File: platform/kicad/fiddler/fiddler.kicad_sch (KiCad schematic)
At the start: 0 parts

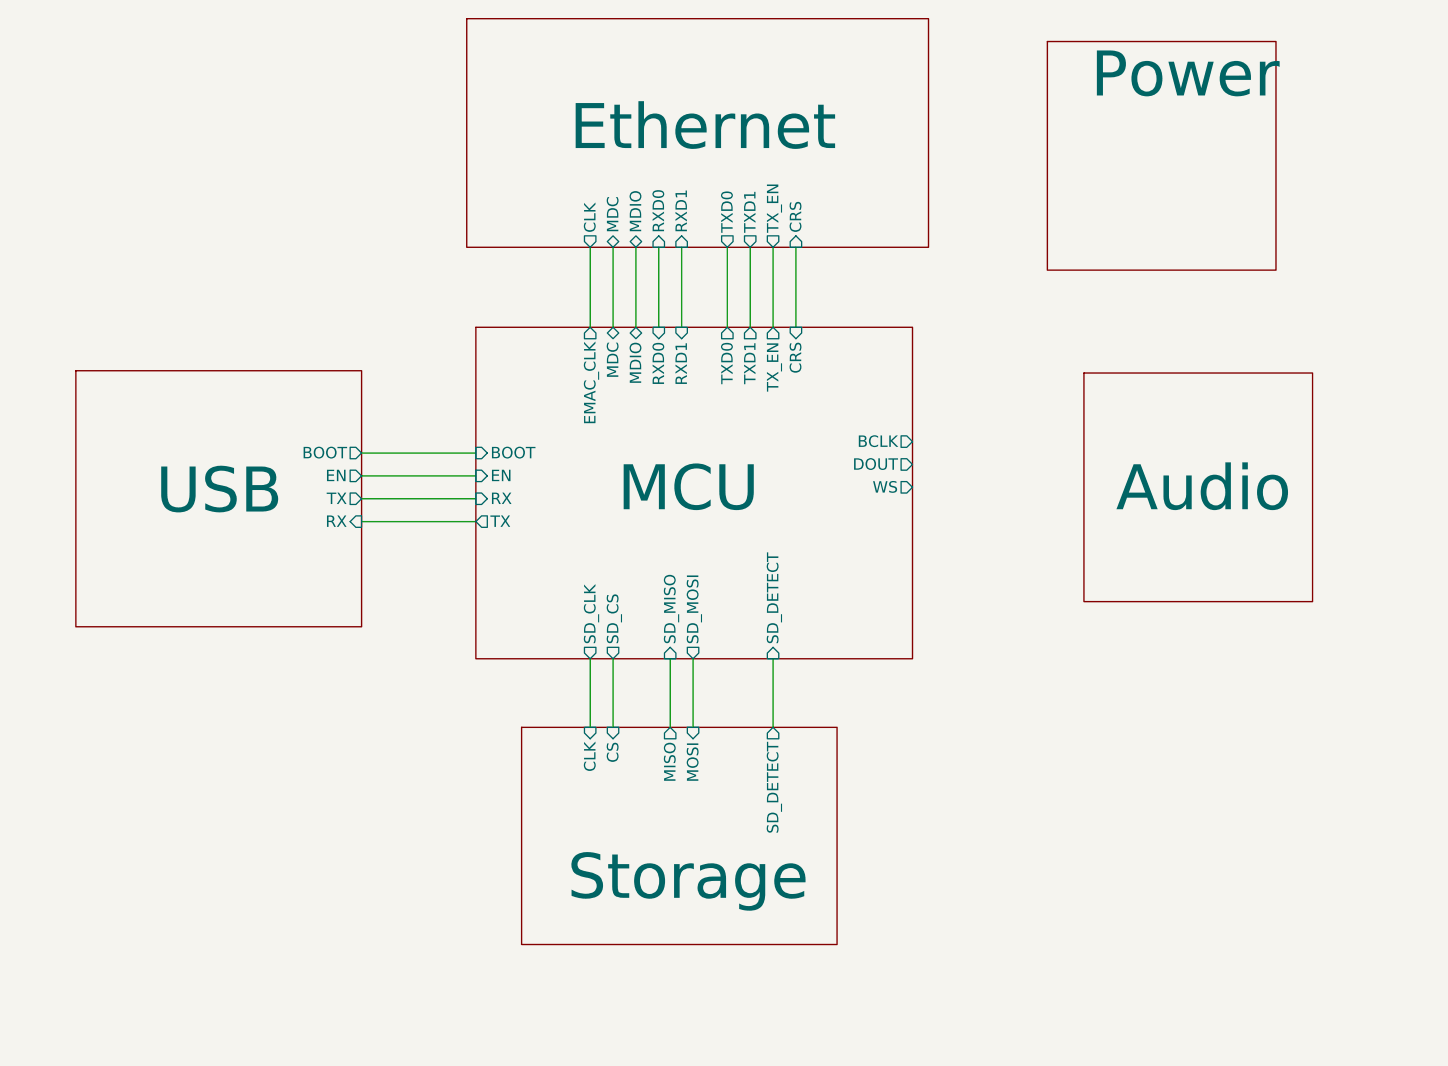
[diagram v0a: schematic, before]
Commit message: Fiddler Ray Speaker: Complete first revision
This change completes the first iteration schematic and layout for the fiddler ray speaker PCB.
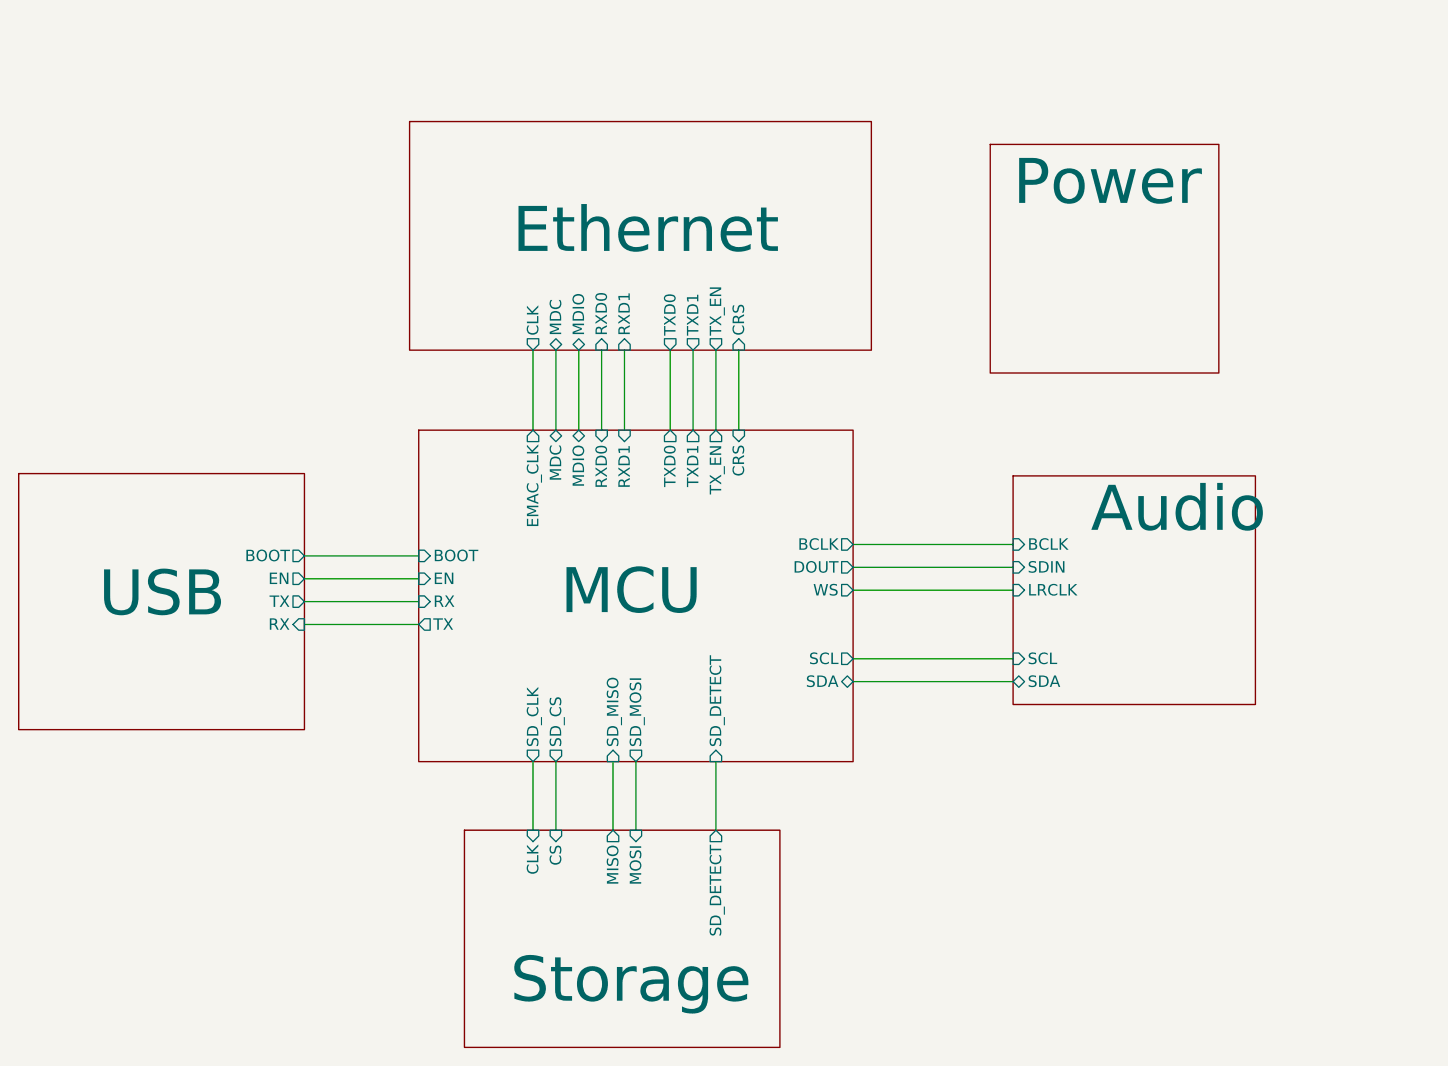
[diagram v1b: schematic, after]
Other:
- sheet Audio ports: added BCLK, LRCLK, SCL, SDA, SDIN; removed none
- sheet MCU ports: added SCL, SDA; removed none
- company: (none) -> The Australian Ocean Laboratory
- title: (none) -> Fiddler Ray Speaker Unit V1

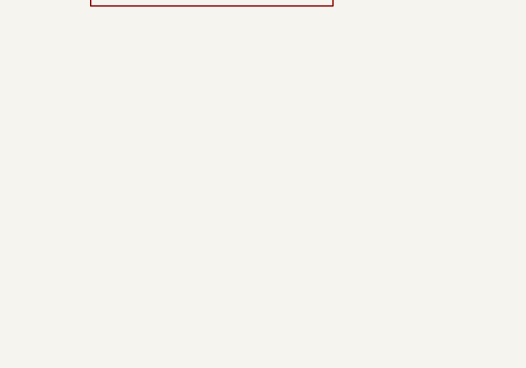
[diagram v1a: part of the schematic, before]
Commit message: Fiddler Ray Speaker: Finalise Silkscreen
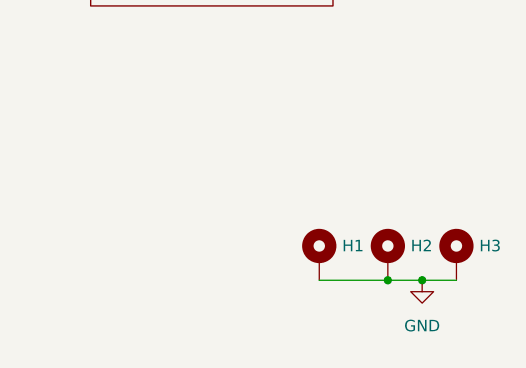
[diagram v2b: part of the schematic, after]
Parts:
- added H1, H2, H3: MountingHole_Pad, MountingHole:MountingHole_3.2mm_M3_DIN965_Pad_TopBottom, symbol Mechanical:MountingHole_Pad
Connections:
- new net GND: H1.1, H2.1, H3.1
